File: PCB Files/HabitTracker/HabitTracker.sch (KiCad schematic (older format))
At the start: 51 parts, among them U1 TLC5955DCA, U2 TLC5955DCA, U3 TLC5955DCA

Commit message: Created PCB and net file
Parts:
- removed LED10, LED37, LED38, LED39, LED40, LED41, LED42, LED43, LED44, LED45, LED46, LED47, LED48, LED7, LED8, LED9: CLP6C-FKB-CKNPRGJBB7A363, footprints:CLP6C-FKB-CKNPRGJBB7A363, symbol 2021-05-25_00-11-51:CLP6C-FKB-CKNPRGJBB7A363
- added LED25, LED26, LED27, LED28: CLP6C-FKB-CKNPRGJBB7A363, footprints:CLP6C-FKB-CKNPRGJBB7A363, symbol 2021-05-25_00-11-51:CLP6C-FKB-CKNPRGJBB7A363
- renumbered LED6 to LED10, LED25 to LED2, LED26 to LED3, LED2 to LED4, LED27 to LED5, LED3 to LED6, LED28 to LED7, LED4 to LED8, LED5 to LED9
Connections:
- net labels removed: SERIAL_LINK2, SERIAL_OUT
- wire segments 759 -> 579

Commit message: Updated PCB
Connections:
- net labels added: SERIAL_LINK2, SERIAL_OUT
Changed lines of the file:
@@
 	29250 6300 30100 6300
 Text Label 27050 6100 0    50   ~ 0
-SERIAL_IN
+SERIAL_LINK2
 Text Label 29550 6100 0    50   ~ 0
-SERIAL_LINK1
+SERIAL_OUT
 Wire Wire Line
 	29250 6100 30100 6100
@@
 	9950 16200 10800 16200
 Text Label 7750 16000 0    50   ~ 0
-SERIAL_IN
+SERIAL_LINK1
 Text Label 10250 16000 0    50   ~ 0
-SERIAL_LINK1
+SERIAL_LINK2
 Wire Wire Line
 	9950 16000 10800 16000

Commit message: First draft of PCB
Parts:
- added C1, C2, C3: 10uF, Capacitor_SMD:C_0805_2012Metric, symbol pspice:CAP
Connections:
- wire segments 579 -> 591
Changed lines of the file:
@@
 L power:+5V #PWR03
 U 1 1 60B06646
-P 8250 6000
-F 0 "#PWR03" H 8250 5850 50  0001 C CNN
-F 1 "+5V" H 8265 6173 50  0000 C CNN
-F 2 "" H 8250 6000 50  0001 C CNN
-F 3 "" H 8250 6000 50  0001 C CNN
-	1    8250 6000
-	1    0    0    -1
-$EndComp
-Wire Wire Line
-	8250 6000 8250 6050
+P 7850 4900
+F 0 "#PWR03" H 7850 4750 50  0001 C CNN
+F 1 "+5V" H 7865 5073 50  0000 C CNN
+F 2 "" H 7850 4900 50  0001 C CNN
+F 3 "" H 7850 4900 50  0001 C CNN
+	1    7850 4900
+	1    0    0    -1
+$EndComp
 Wire Wire Line
 	8250 6050 8300 6050
@@
 Wire Wire Line
 	27600 5900 27650 5900
-Wire Wire Line
-	27600 5850 27600 5900
-$Comp
-L power:+5V #PWR011
-U 1 1 63311B96
-P 27600 5850
-F 0 "#PWR011" H 27600 5700 50  0001 C CNN
-F 1 "+5V" H 27615 6023 50  0000 C CNN
-F 2 "" H 27600 5850 50  0001 C CNN
-F 3 "" H 27600 5850 50  0001 C CNN
-	1    27600 5850
-	1    0    0    -1
-$EndComp
 Text Label 29650 6300 0    50   ~ 0
 GS_CLOCK
@@
 Wire Wire Line
 	8300 15800 8350 15800
-Wire Wire Line
-	8300 15750 8300 15800
-$Comp
-L power:+5V #PWR07
-U 1 1 62BB05AC
-P 8300 15750
-F 0 "#PWR07" H 8300 15600 50  0001 C CNN
-F 1 "+5V" H 8315 15923 50  0000 C CNN
-F 2 "" H 8300 15750 50  0001 C CNN
-F 3 "" H 8300 15750 50  0001 C CNN
-	1    8300 15750
-	1    0    0    -1
-$EndComp
 Text Label 10350 16200 0    50   ~ 0
 GS_CLOCK
@@
 	-1   0    0    -1
 $EndComp
+$Comp
+L pspice:CAP C1
+U 1 1 612B4CA5
+P 7850 5250
+F 0 "C1" H 8028 5296 50  0000 L CNN
+F 1 "10uF" H 8028 5205 50  0000 L CNN
+F 2 "Capacitor_SMD:C_0805_2012Metric" H 7850 5250 50  0001 C CNN
+F 3 "~" H 7850 5250 50  0001 C CNN
+	1    7850 5250
+	1    0    0    -1
+$EndComp
+Wire Wire Line
+	7850 4900 7850 4950
+Connection ~ 7850 4950
+Wire Wire Line
+	7850 4950 7850 5000
+Wire Wire Line
+	7850 4950 8250 4950
+Wire Wire Line
+	8250 4950 8250 6050
+$Comp
+L power:GND #PWR0101
+U 1 1 61546A2D
+P 7850 5650
+F 0 "#PWR0101" H 7850 5400 50  0001 C CNN
+F 1 "GND" H 7855 5477 50  0000 C CNN
+F 2 "" H 7850 5650 50  0001 C CNN
+F 3 "" H 7850 5650 50  0001 C CNN
+	1    7850 5650
+	1    0    0    -1
+$EndComp
+Wire Wire Line
+	7850 5500 7850 5650
+$Comp
+L power:+5V #PWR07
+U 1 1 615BBD7E
+P 27200 4950
+F 0 "#PWR07" H 27200 4800 50  0001 C CNN
+F 1 "+5V" H 27215 5123 50  0000 C CNN
+F 2 "" H 27200 4950 50  0001 C CNN
+F 3 "" H 27200 4950 50  0001 C CNN
+	1    27200 4950
+	1    0    0    -1
+$EndComp
+$Comp
+L pspice:CAP C2
+U 1 1 615BBD84
+P 27200 5300
+F 0 "C2" H 27378 5346 50  0000 L CNN
+F 1 "10uF" H 27378 5255 50  0000 L CNN
+F 2 "Capacitor_SMD:C_0805_2012Metric" H 27200 5300 50  0001 C CNN
+F 3 "~" H 27200 5300 50  0001 C CNN
+	1    27200 5300
+	1    0    0    -1
+$EndComp
+Wire Wire Line
+	27200 4950 27200 5000
+Connection ~ 27200 5000
+Wire Wire Line
+	27200 5000 27200 5050
+Wire Wire Line
+	27200 5000 27600 5000
+$Comp
+L power:GND #PWR011
+U 1 1 615BBD8E
+P 27200 5700
+F 0 "#PWR011" H 27200 5450 50  0001 C CNN
+F 1 "GND" H 27205 5527 50  0000 C CNN
+F 2 "" H 27200 5700 50  0001 C CNN
+F 3 "" H 27200 5700 50  0001 C CNN
+	1    27200 5700
+	1    0    0    -1
+$EndComp
+Wire Wire Line
+	27200 5550 27200 5700
+Wire Wire Line
+	27600 5000 27600 5900
+$Comp
+L power:+5V #PWR013
+U 1 1 61707D51
+P 7900 14900
+F 0 "#PWR013" H 7900 14750 50  0001 C CNN
+F 1 "+5V" H 7915 15073 50  0000 C CNN
+F 2 "" H 7900 14900 50  0001 C CNN
+F 3 "" H 7900 14900 50  0001 C CNN
+	1    7900 14900
+	1    0    0    -1
+$EndComp
+$Comp
+L pspice:CAP C3
+U 1 1 61707D57
+P 7900 15250
+F 0 "C3" H 8078 15296 50  0000 L CNN
+F 1 "10uF" H 8078 15205 50  0000 L CNN
+F 2 "Capacitor_SMD:C_0805_2012Metric" H 7900 15250 50  0001 C CNN
+F 3 "~" H 7900 15250 50  0001 C CNN
+	1    7900 15250
+	1    0    0    -1
+$EndComp
+Wire Wire Line
+	7900 14900 7900 14950
+Connection ~ 7900 14950
+Wire Wire Line
+	7900 14950 7900 15000
+Wire Wire Line
+	7900 14950 8300 14950
+$Comp
+L power:GND #PWR014
+U 1 1 61707D61
+P 7900 15650
+F 0 "#PWR014" H 7900 15400 50  0001 C CNN
+F 1 "GND" H 7905 15477 50  0000 C CNN
+F 2 "" H 7900 15650 50  0001 C CNN
+F 3 "" H 7900 15650 50  0001 C CNN
+	1    7900 15650
+	1    0    0    -1
+$EndComp
+Wire Wire Line
+	7900 15500 7900 15650
+Wire Wire Line
+	8300 14950 8300 15800
 $EndSCHEMATC

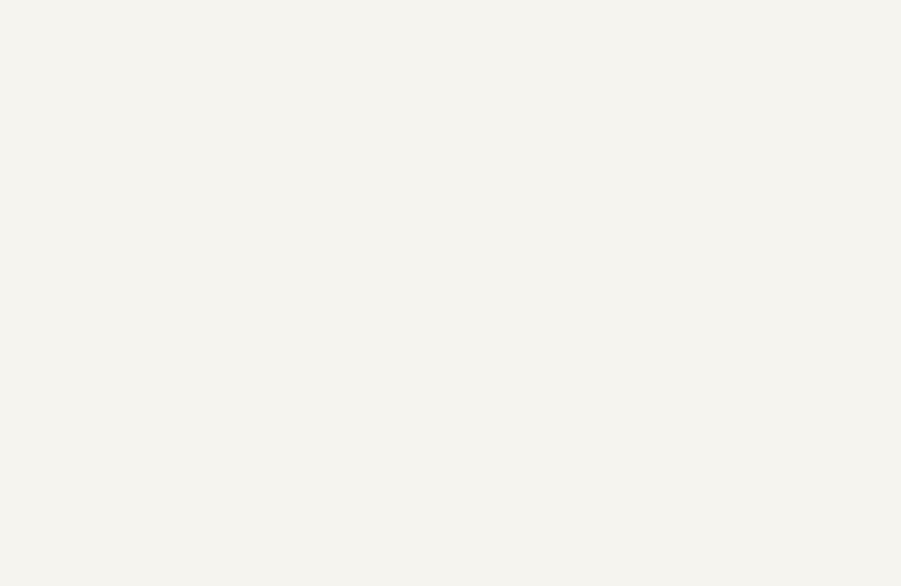
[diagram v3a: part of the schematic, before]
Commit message: Added connector to PCB
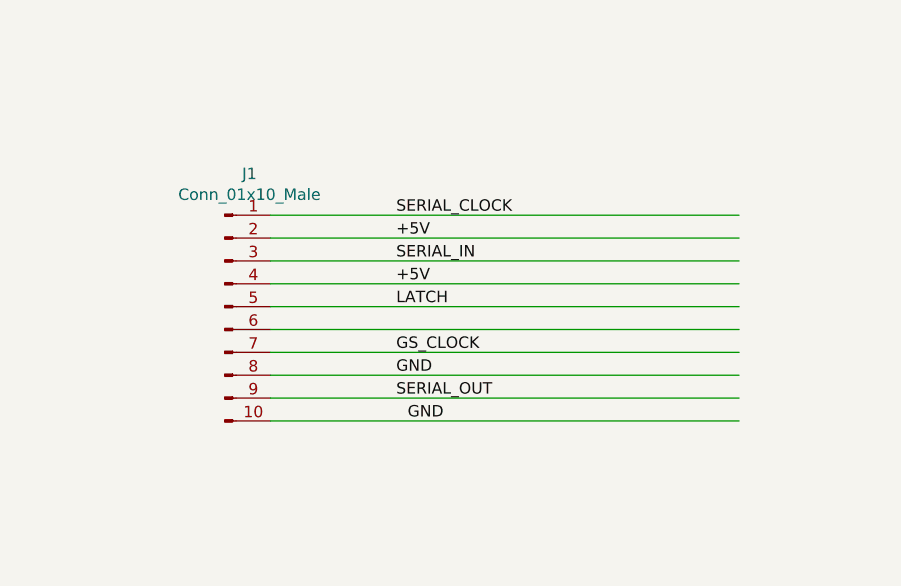
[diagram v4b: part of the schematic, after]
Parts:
- added J1: Conn_01x10_Male, Connector_PinSocket_2.54mm:PinSocket_2x05_P2.54mm_Vertical, symbol Connector:Conn_01x10_Male
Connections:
- wire segments 591 -> 601
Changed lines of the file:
@@
 Wire Wire Line
 	8300 14950 8300 15800
+$Comp
+L Connector:Conn_01x10_Male J1
+U 1 1 6182C739
+P 22750 14200
+F 0 "J1" H 22858 14781 50  0000 C CNN
+F 1 "Conn_01x10_Male" H 22858 14690 50  0000 C CNN
+F 2 "Connector_PinSocket_2.54mm:PinSocket_2x05_P2.54mm_Vertical" H 22750 14200 50  0001 C CNN
+F 3 "~" H 22750 14200 50  0001 C CNN
+	1    22750 14200
+	1    0    0    -1
+$EndComp
+Wire Wire Line
+	22950 13800 25000 13800
+Wire Wire Line
+	22950 13900 25000 13900
+Wire Wire Line
+	22950 14100 25000 14100
+Wire Wire Line
+	22950 14200 25000 14200
+Wire Wire Line
+	22950 14300 25000 14300
+Wire Wire Line
+	22950 14400 25000 14400
+Wire Wire Line
+	22950 14500 25000 14500
+Wire Wire Line
+	22950 14600 25000 14600
+Wire Wire Line
+	22950 14700 25000 14700
+Text Label 23500 13900 0    50   ~ 0
++5V
+Text Label 23500 14100 0    50   ~ 0
++5V
+Wire Wire Line
+	22950 14000 25000 14000
+Text Label 23500 14500 0    50   ~ 0
+GND
+Text Label 23550 14700 0    50   ~ 0
+GND
+Text Label 23500 14200 0    50   ~ 0
+LATCH
+Text Label 23500 13800 0    50   ~ 0
+SERIAL_CLOCK
+Text Label 23500 14000 0    50   ~ 0
+SERIAL_IN
+Text Label 23500 14600 0    50   ~ 0
+SERIAL_OUT
+Text Label 23500 14400 0    50   ~ 0
+GS_CLOCK
 $EndSCHEMATC
